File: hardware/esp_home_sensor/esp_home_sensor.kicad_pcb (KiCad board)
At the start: 2 copper layers, 6 parts, among them J2 Conn_01x04_MountingPin, J3 Conn_01x04_MountingPin, J4 Conn_01x08_MountingPin, U6 ESP32-C6-MINI-1, U7 BME680

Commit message: minor update
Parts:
- added BT1: Battery_Cell, Battery:BatteryHolder_Keystone_1042_1x18650, B.Cu at (132.9, 111.5)
- added C1: 1u, Capacitor_SMD:C_0402_1005Metric, F.Cu at (208.3, 120.4)
- added C10: 100n, Capacitor_SMD:C_0402_1005Metric, F.Cu at (166.6, 142.5)
- added C11: 100n, Capacitor_SMD:C_0402_1005Metric, F.Cu at (166.6, 144.5)
- added C12: 4.7u, Capacitor_SMD:C_0402_1005Metric, F.Cu at (205.2, 110.5)
- added C13: 4.7u, Capacitor_SMD:C_0402_1005Metric, F.Cu at (205.2, 112.5)
- added C14: 100n, Capacitor_SMD:C_0402_1005Metric, F.Cu at (176.7, 141.4)
- added C15: 100n, Capacitor_SMD:C_0402_1005Metric, F.Cu at (205.2, 114.4)
- added C16: 100n, Capacitor_SMD:C_0402_1005Metric, F.Cu at (205.2, 116.4)
- added C17: 4.7u, Capacitor_SMD:C_0402_1005Metric, F.Cu at (201.1, 134.3)
- added C18: 10u, Capacitor_SMD:C_0402_1005Metric, F.Cu at (201.1, 136.3)
- added C19: 4.7u, Capacitor_SMD:C_0402_1005Metric, F.Cu at (201.1, 138.3)
- added C2: 1u, Capacitor_SMD:C_0402_1005Metric, F.Cu at (208.3, 122.4)
- added C20: 10u, Capacitor_SMD:C_0402_1005Metric, F.Cu at (201.1, 140.2)
- added C3: 100n, Capacitor_SMD:C_0402_1005Metric, F.Cu at (187.5, 140.7)
- added C4: 100n, Capacitor_SMD:C_0402_1005Metric, F.Cu at (187.5, 142.7)
- added C9: 1u, Capacitor_SMD:C_0402_1005Metric, F.Cu at (205.2, 108.5)
- added D1: LED, LED_SMD:LED_0402_1005Metric, F.Cu at (208.6, 127.5)
- added D2: LED, LED_SMD:LED_0402_1005Metric, F.Cu at (208.6, 129.5)
- added J1: USB_C_Receptacle_USB2.0_16P, Connector_USB:USB_C_Receptacle_GCT_USB4110, F.Cu at (168.2, 100.9)
- added JP1: SolderJumper_3_Bridged12, Jumper:SolderJumper-3_P1.3mm_Bridged12_Pad1.0x1.5mm, F.Cu at (162.3, 138.4)
- added JP2: SolderJumper_3_Bridged12, Jumper:SolderJumper-3_P1.3mm_Bridged12_Pad1.0x1.5mm, F.Cu at (209.4, 109.3)
- added JP3: SolderJumper_3_Bridged12, Jumper:SolderJumper-3_P1.3mm_Bridged12_Pad1.0x1.5mm, F.Cu at (162.3, 142.2)
- added JP4: SolderJumper_3_Bridged12, Jumper:SolderJumper-3_P1.3mm_Bridged12_Pad1.0x1.5mm, F.Cu at (174.5, 138.4)
- added JP6: SolderJumper_2_Bridged, Jumper:SolderJumper-2_P1.3mm_Bridged2Bar_Pad1.0x1.5mm, F.Cu at (204.7, 121.2)
- added JP7: SolderJumper_2_Open, Jumper:SolderJumper-2_P1.3mm_Open_Pad1.0x1.5mm, F.Cu at (208.2, 140.6)
- added JP8: SolderJumper_2_Bridged, Jumper:SolderJumper-2_P1.3mm_Bridged2Bar_Pad1.0x1.5mm, F.Cu at (204.7, 124.7)
- added L1: 2.2u, Inductor_SMD:L_0805_2012Metric, F.Cu at (208.3, 134.7)
- added L2: 2.2u, Inductor_SMD:L_0805_2012Metric, F.Cu at (208.3, 137.5)
- added R1: 680, Resistor_SMD:R_0402_1005Metric, F.Cu at (201.1, 120.4)
- added R10: 1k, Resistor_SMD:R_0402_1005Metric, F.Cu at (184.7, 142.3)
- added R11: 1k, Resistor_SMD:R_0402_1005Metric, F.Cu at (184.7, 144.3)
- added R12: 100k, Resistor_SMD:R_0402_1005Metric, F.Cu at (208.1, 115.9)
- added R13: 5.1k, Resistor_SMD:R_0402_1005Metric, F.Cu at (184.7, 130.4)
- added R14: 5.1k, Resistor_SMD:R_0402_1005Metric, F.Cu at (184.7, 132.4)
- added R15: 270k, Resistor_SMD:R_0402_1005Metric, F.Cu at (204.0, 140.8)
- added R16: 270k, Resistor_SMD:R_0402_1005Metric, F.Cu at (204.0, 142.8)
- added R2: 27k, Resistor_SMD:R_0402_1005Metric, F.Cu at (201.1, 122.4)
- added R3: 10k, Resistor_SMD:R_0402_1005Metric, F.Cu at (201.1, 124.4)
- added R4: 10k, Resistor_SMD:R_0402_1005Metric, F.Cu at (201.1, 126.4)
- added R5: R, Resistor_SMD:R_0402_1005Metric, F.Cu at (201.1, 128.4)
- added R6: R, Resistor_SMD:R_0402_1005Metric, F.Cu at (201.1, 130.3)
- added R7: 15, Resistor_SMD:R_0402_1005Metric, F.Cu at (184.7, 136.4)
- added R8: 100, Resistor_SMD:R_0402_1005Metric, F.Cu at (184.7, 138.4)
- added R9: 15, Resistor_SMD:R_0402_1005Metric, F.Cu at (184.7, 140.3)
- added SW1: SW_Push, Button_Switch_SMD:SW_SPST_Omron_B3FS-101xP, F.Cu at (209.4, 87.9)
- added SW2: SW_Push, Button_Switch_SMD:SW_SPST_Omron_B3FS-101xP, F.Cu at (209.4, 95.8)
- added SW3: SW_Push, Button_Switch_SMD:SW_SPST_Omron_B3FS-101xP, F.Cu at (209.4, 103.6)
- added TH1: NTCSP163JF103FT1H, Resistor_SMD:R_0603_1608Metric, F.Cu at (208.9, 124.6)
- added U1: BQ25170, esp_home_sensor:QFN-8_EP_2x2_Pitch0.5mm, F.Cu at (204.7, 128.7)
- added U10: TPS62840, esp_home_sensor:BGA-6_2x3_1.5x1.2mm, F.Cu at (204.3, 138.2)
- added U2: BQ2970, esp_home_sensor:QFN-8_1.5x1.5_Pitch0.5mm, F.Cu at (190.9, 141.6)
- added U3: IRLHS6276TRPBF, esp_home_sensor:QFN-6_2x2_Pitch0.65mm, F.Cu at (188.3, 137.5)
- added U8: VEML3235, esp_home_sensor:VEML3235, F.Cu at (173.6, 142.3)
- added U9: TPS62840, esp_home_sensor:BGA-6_2x3_1.5x1.2mm, F.Cu at (204.3, 135.0)
- moved D3 84.3 mm to (208.8, 113.2)
- moved U6 55.1 mm to (88.6, 86.0), turned to 90 degrees
- moved J2 39.9 mm to (163.9, 123.2)
- moved J3 39.9 mm to (163.9, 130.8)
- moved J4 39.9 mm to (174.8, 123.2)
- moved U7 34.4 mm to (167.4, 139.2)

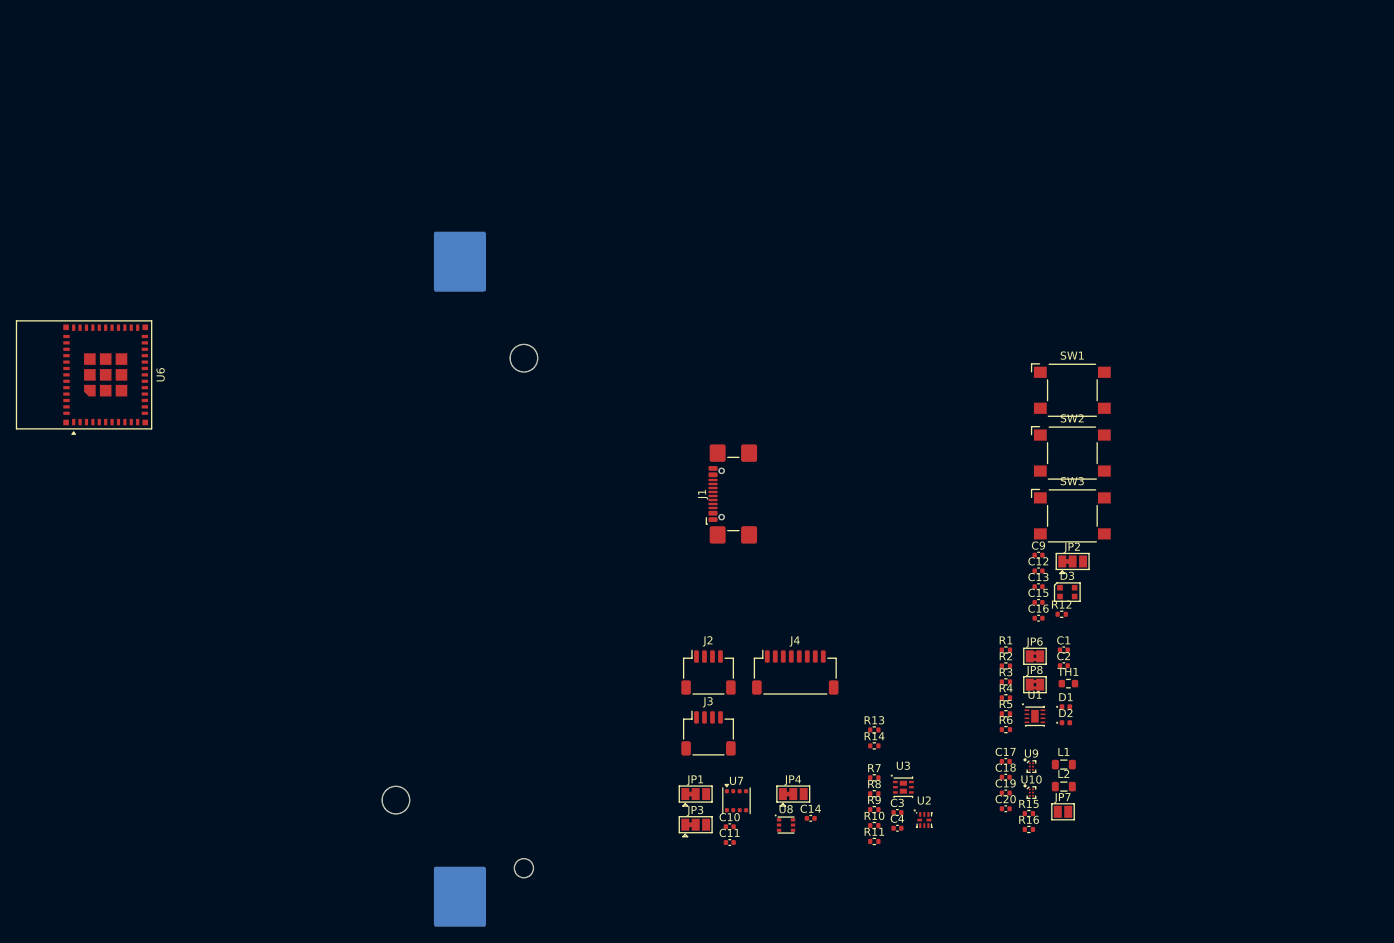
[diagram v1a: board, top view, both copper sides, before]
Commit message: initial layout, power routing
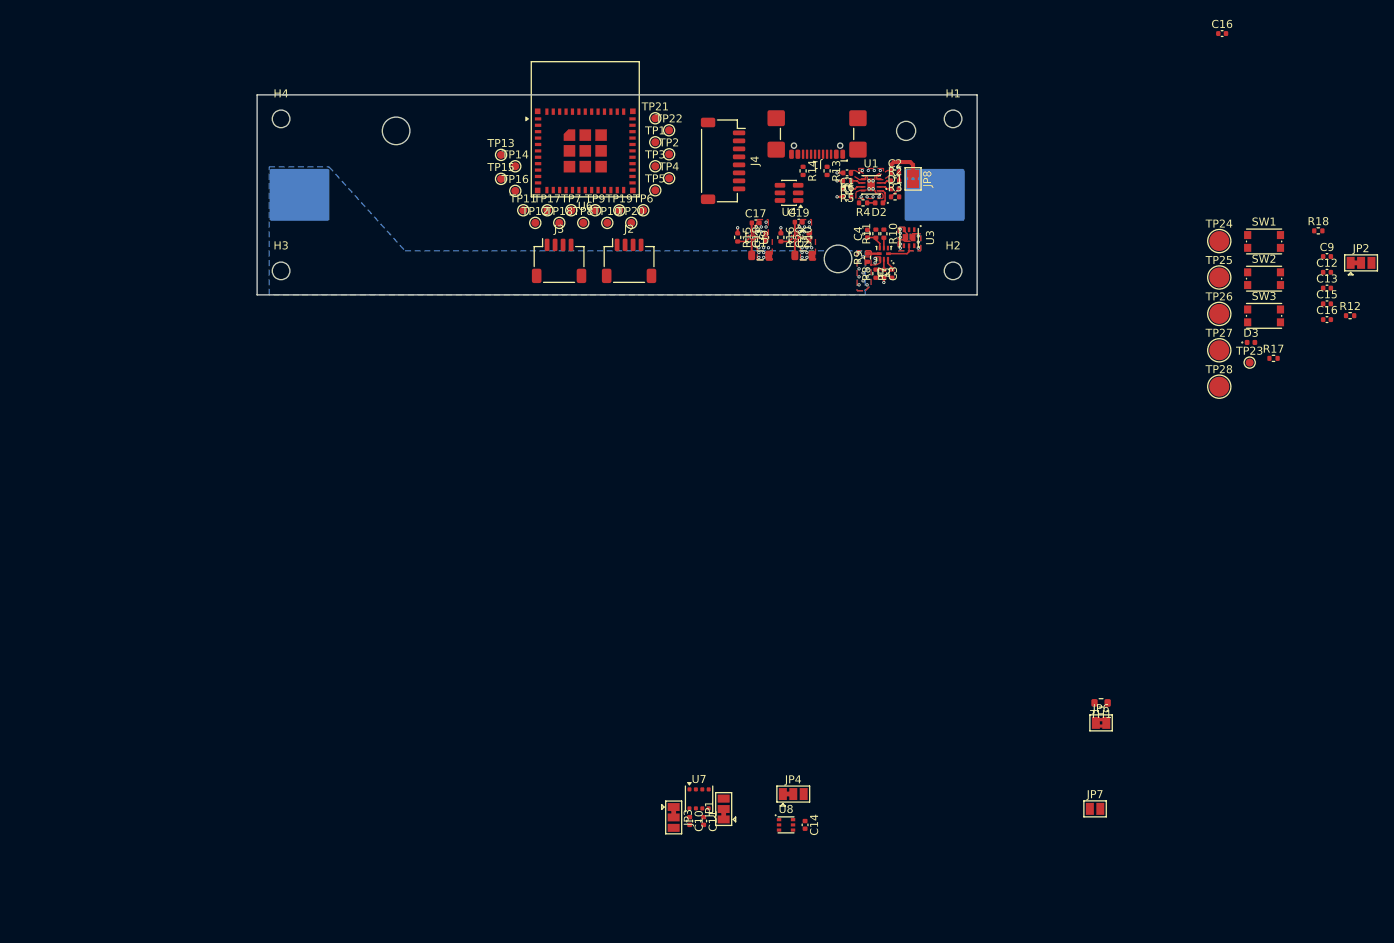
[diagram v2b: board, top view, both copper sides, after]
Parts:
- added C16: 100n, Capacitor_SMD:C_0402_1005Metric, F.Cu at (228.1, 43.3)
- added H1: MountingHole, MountingHole:MountingHole_2.2mm_M2, F.Cu at (194.5, 54.0)
- added H2: MountingHole, MountingHole:MountingHole_2.2mm_M2, F.Cu at (194.5, 73.0)
- added H3: MountingHole, MountingHole:MountingHole_2.2mm_M2, F.Cu at (110.5, 73.0)
- added H4: MountingHole, MountingHole:MountingHole_2.2mm_M2, F.Cu at (110.5, 54.0)
- added R17: 10k, Resistor_SMD:R_0402_1005Metric, F.Cu at (234.6, 83.9)
- added R18: 100, Resistor_SMD:R_0402_1005Metric, F.Cu at (240.2, 68.0)
- added TP1: TestPoint, TestPoint:TestPoint_Pad_D1.0mm, F.Cu at (157.3, 56.9)
- added TP10: TestPoint, TestPoint:TestPoint_Pad_D1.0mm, F.Cu at (151.3, 67.0)
- added TP11: TestPoint, TestPoint:TestPoint_Pad_D1.0mm, F.Cu at (140.8, 65.4)
- added TP12: TestPoint, TestPoint:TestPoint_Pad_D1.0mm, F.Cu at (142.3, 67.0)
- added TP13: TestPoint, TestPoint:TestPoint_Pad_D1.0mm, F.Cu at (138.0, 58.5)
- added TP14: TestPoint, TestPoint:TestPoint_Pad_D1.0mm, F.Cu at (139.8, 59.9)
- added TP15: TestPoint, TestPoint:TestPoint_Pad_D1.0mm, F.Cu at (138.0, 61.5)
- added TP16: TestPoint, TestPoint:TestPoint_Pad_D1.0mm, F.Cu at (139.8, 63.0)
- added TP17: TestPoint, TestPoint:TestPoint_Pad_D1.0mm, F.Cu at (143.8, 65.4)
- added TP18: TestPoint, TestPoint:TestPoint_Pad_D1.0mm, F.Cu at (145.3, 67.0)
- added TP19: TestPoint, TestPoint:TestPoint_Pad_D1.0mm, F.Cu at (152.8, 65.4)
- added TP2: TestPoint, TestPoint:TestPoint_Pad_D1.0mm, F.Cu at (159.0, 58.4)
- added TP20: TestPoint, TestPoint:TestPoint_Pad_D1.0mm, F.Cu at (154.3, 67.0)
- added TP21: TestPoint, TestPoint:TestPoint_Pad_D1.0mm, F.Cu at (157.3, 53.9)
- added TP22: TestPoint, TestPoint:TestPoint_Pad_D1.0mm, F.Cu at (159.0, 55.4)
- added TP23: TestPoint, TestPoint:TestPoint_Pad_D1.0mm, F.Cu at (231.6, 84.5)
- added TP24: TestPoint, TestPoint:TestPoint_Pad_D2.5mm, F.Cu at (227.8, 69.3)
- added TP25: TestPoint, TestPoint:TestPoint_Pad_D2.5mm, F.Cu at (227.8, 73.8)
- added TP26: TestPoint, TestPoint:TestPoint_Pad_D2.5mm, F.Cu at (227.8, 78.4)
- added TP27: TestPoint, TestPoint:TestPoint_Pad_D2.5mm, F.Cu at (227.8, 82.9)
- added TP28: TestPoint, TestPoint:TestPoint_Pad_D2.5mm, F.Cu at (227.8, 87.5)
- added TP3: TestPoint, TestPoint:TestPoint_Pad_D1.0mm, F.Cu at (157.3, 59.9)
- added TP4: TestPoint, TestPoint:TestPoint_Pad_D1.0mm, F.Cu at (159.0, 61.4)
- added TP5: TestPoint, TestPoint:TestPoint_Pad_D1.0mm, F.Cu at (157.3, 62.9)
- added TP6: TestPoint, TestPoint:TestPoint_Pad_D1.0mm, F.Cu at (155.8, 65.4)
- added TP7: TestPoint, TestPoint:TestPoint_Pad_D1.0mm, F.Cu at (146.8, 65.4)
- added TP8: TestPoint, TestPoint:TestPoint_Pad_D1.0mm, F.Cu at (148.3, 67.0)
- added TP9: TestPoint, TestPoint:TestPoint_Pad_D1.0mm, F.Cu at (149.8, 65.4)
- added U4: WE-TVS-82400102, Package_TO_SOT_SMD:SOT-23-6, F.Cu at (174.0, 63.2)
- D3: value WS2812B-2020 -> LED; footprint LED_SMD:LED_WS2812B-2020_PLCC4_2.0x2.0mm -> LED_SMD:LED_0402_1005Metric
- SW1, SW2, SW3: footprint Button_Switch_SMD:SW_SPST_Omron_B3FS-101xP -> Button_Switch_SMD:SW_Push_1P1T_NO_CK_KMR2
- moved R15 80.7 mm to (167.6, 68.8), turned to -90 degrees
- moved R16 80.2 mm to (173.0, 68.8), turned to -90 degrees
- moved R11 76.0 mm to (184.8, 68.3), turned to 90 degrees
- moved C19 75.9 mm to (175.2, 66.9)
- moved C20 75.5 mm to (176.5, 68.8), turned to 90 degrees
- moved U10 75.4 mm to (174.7, 68.8), turned to -90 degrees
- moved U9 74.8 mm to (169.3, 68.8), turned to -90 degrees
- moved C4 74.4 mm to (183.8, 68.3), turned to 90 degrees
- moved C17 74.2 mm to (169.8, 67.0)
- moved L1 74.1 mm to (170.4, 71.1)
- moved R10 74.0 mm to (185.8, 68.3), turned to -90 degrees
- moved L2 74.0 mm to (175.8, 71.1)
- moved C18 73.9 mm to (171.1, 68.8), turned to 90 degrees
- moved R14 72.4 mm to (175.8, 60.5), turned to -90 degrees
- moved U2 71.0 mm to (185.8, 70.8), turned to 180 degrees
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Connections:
- net /MCU/3V3_EN renamed /DC_DC/EN
- net Net-(J1-CC1) renamed /USB/usb_cc1
- net Net-(J1-CC2) renamed /USB/usb_cc2
- net Net-(JP1-C) renamed /Env_sensor/sdo
- net Net-(U1-ISET) renamed /Charger/ISET
- net Net-(U1-VSET) renamed /Charger/VSET
- net Net-(U2-BAT) renamed /Protection/BAT
- net Net-(U2-CHG) renamed /Protection/CHG
- net Net-(U2-CTR) renamed /Protection/CTR
- net Net-(U2-DSG) renamed /Protection/DSG
- net Net-(U2-PACK) renamed /Protection/PACK
- net Net-(U2-VDD) renamed /Protection/VDD
- C2 pad 1: VBAT -> /Charger/OUT
- D3 pad 1: unconnected-(D3-DOUT-Pad1) -> /MCU/USER_LED
- D3 pad 2: GND -> Net-(D3-A)
- J1 pad A6: /MCU/USB.USB_P -> /USB/USB_P
- J1 pad A7: /MCU/USB.USB_N -> /USB/USB_N
- J1 pad B6: /MCU/USB.USB_P -> /USB/USB_P
- J1 pad B7: /MCU/USB.USB_N -> /USB/USB_N
- JP8 pad 1: Net-(JP8-A) -> /Charger/OUT
- L1 pad 1: Net-(U9-SW) -> /DC_DC/SW
- L2 pad 1: Net-(U10-SW) -> /DC_DC/SW
- R15 pad 2: Net-(U9-VSET) -> /DC_DC/VSET
- R16 pad 2: Net-(U10-VSET) -> /DC_DC/VSET
- R3 pad 2: Net-(JP8-A) -> /Charger/OUT
- R4 pad 2: Net-(JP8-A) -> /Charger/OUT
- U1 pad 8: Net-(JP8-A) -> /Charger/OUT
- U10 pad 2B: Net-(U10-SW) -> /DC_DC/SW
- U10 pad 2C: Net-(U10-VSET) -> /DC_DC/VSET
- U6 pad 10: unconnected-(U6-IO5-Pad10) -> /MCU/IO5
- U6 pad 12: /MCU/LED_DATA -> /MCU/USER_LED
- U6 pad 15: unconnected-(U6-IO6-Pad15) -> /MCU/IO6
- U6 pad 16: unconnected-(U6-IO7-Pad16) -> /MCU/IO7
- U6 pad 22: unconnected-(U6-IO8-Pad22) -> /MCU/IO8
- U6 pad 5: VBAT -> /MCU/ADC_BAT
- U6 pad 9: unconnected-(U6-IO4-Pad9) -> /MCU/IO4
- U9 pad 2B: Net-(U9-SW) -> /DC_DC/SW
- U9 pad 2C: Net-(U9-VSET) -> /DC_DC/VSET
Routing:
- net GND: track 0.00 -> 6.00 mm, vias 0 -> 33
- net /Charger/OUT: track 0.00 -> 5.13 mm
- net /DC_DC/SW: track 0.00 -> 4.10 mm
- net /Protection/CHG: track 0.00 -> 3.43 mm
- net VBAT: track 0.00 -> 3.40 mm, vias 0 -> 3
- net /DC_DC/VSET: track 0.00 -> 2.96 mm
- net /Charger/TS: track 0.00 -> 2.59 mm
- net /Protection/CTR: track 0.00 -> 2.55 mm
- net /Protection/VDD: track 0.00 -> 2.33 mm
- net /Charger/STAT: track 0.00 -> 2.21 mm
- net /Charger//PG: track 0.00 -> 1.62 mm
- net /Charger/VSET: track 0.00 -> 1.59 mm
- net /Charger/ISET: track 0.00 -> 1.59 mm
- net /Protection/BAT: track 0.00 -> 1.49 mm
- net /Protection/BAT-: track 0.00 -> 1.48 mm, vias 0 -> 11
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- added copper zone on F.Cu, net /Charger/OUT
- added copper zone on F.Cu, net /Charger/VIN
- added copper zone on B.Cu, net /Protection/BAT-
- added copper zone on F.Cu, net /Protection/BAT-
- added copper zone on F.Cu, net 3V3_AUX
- added copper zone on F.Cu, net 3V3_MCU
- added copper zone on F.Cu, net GND
- added copper zone on In1.Cu, net GND
- added copper zone on B.Cu, net Net-(U3-Pad4)
- added copper zone on F.Cu, net Net-(U3-Pad4)
- added copper zone on In2.Cu, net Net-(U3-Pad4)
- added copper zone on B.Cu, net VBAT
- added copper zone on F.Cu, net VBAT
- added copper zone on In2.Cu, net VBAT
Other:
- board outline added: 90 x 25 mm
- copper layers 2 -> 4
- rule pad_to_mask_clearance: 0 -> 0.05

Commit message: layout
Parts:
- removed the C16 at (241.2, 79.1)
- removed JP2: SolderJumper_3_Bridged12, Jumper:SolderJumper-3_P1.3mm_Bridged12_Pad1.0x1.5mm
- removed TP26: TestPoint, TestPoint:TestPoint_Pad_D2.5mm
- added TP29: TestPoint, TestPoint:TestPoint_Pad_D2.5mm, F.Cu at (115.5, 54.0)
- added TP30: TestPoint, TestPoint:TestPoint_Pad_D2.5mm, F.Cu at (162.5, 73.8)
- TH1: moved to B.Cu
- moved R12 109.8 mm to (136.0, 59.5)
- moved C9 105.8 mm to (136.0, 60.5), turned to 180 degrees
- moved C15 104.9 mm to (136.5, 72.0), turned to -90 degrees
- moved R18 103.0 mm to (137.8, 56.8), turned to 180 degrees
- moved C13 102.8 mm to (140.5, 54.6), turned to 180 degrees
- moved C12 102.3 mm to (140.5, 55.6), turned to 180 degrees
- moved R17 98.6 mm to (137.7, 65.7), turned to -90 degrees
- moved TP23 94.8 mm to (140.0, 60.0)
- moved C14 94.7 mm to (130.3, 59.3), turned to 90 degrees
- moved D3 94.4 mm to (138.7, 65.7), turned to -90 degrees
- moved SW3 93.6 mm to (140.0, 72.0), turned to 180 degrees
- moved JP4 91.4 mm to (128.0, 59.8), turned to 90 degrees
- moved U8 90.9 mm to (131.0, 62.0), turned to 90 degrees
- moved C10 90.5 mm to (121.1, 60.8), turned to 180 degrees
- moved JP1 90.4 mm to (118.5, 63.2)
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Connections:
- L1 pad 1: /DC_DC/SW -> /DC_DC/SW_mcu
- L2 pad 1: /DC_DC/SW -> /DC_DC/SW_aux
- TP25 pad 1: /MCU/PROG_RX -> 3V3_AUX
- U10 pad 2B: /DC_DC/SW -> /DC_DC/SW_aux
- U4 pad 1: /USB/USB_P -> /USB/USB_N
- U4 pad 3: /USB/USB_N -> /USB/USB_P
- U4 pad 4: /MCU/USB.USB_N -> /MCU/USB.USB_P
- U4 pad 6: /MCU/USB.USB_P -> /MCU/USB.USB_N
- U9 pad 2B: /DC_DC/SW -> /DC_DC/SW_mcu
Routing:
- net VBAT: track 3.40 -> 85.9 mm, vias 3 -> 6
- net /Env_sensor/I2C.SCL: track 0.00 -> 67.1 mm, vias 0 -> 2
- net /Env_sensor/I2C.SDA: track 0.00 -> 63.1 mm, vias 0 -> 2
- net /DC_DC/EN: track 0.00 -> 40.9 mm, vias 0 -> 2
- net GND: track 6.00 -> 42.7 mm, vias 33 -> 91
- net /MCU/USB.USB_N: track 0.00 -> 36.2 mm
- net /MCU/USB.USB_P: track 0.00 -> 35.5 mm
- net 3V3_AUX: track 0.00 -> 29.5 mm, vias 7 -> 11
- net /MCU/EN: track 0.00 -> 24.6 mm, vias 0 -> 2
- net /MCU/USER_SW: track 0.00 -> 23.2 mm, vias 0 -> 2
- net /MCU/DISP_IF.CLK: track 0.00 -> 18.2 mm, vias 0 -> 2
- net /Charger/VIN: track 0.00 -> 16.3 mm
- net /MCU/BOOT: track 0.00 -> 15.2 mm, vias 0 -> 2
- net /MCU/DISP_IF.BUSY: track 0.00 -> 14.9 mm
- net /MCU/DISP_IF.MOSI: track 0.00 -> 14.6 mm
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- added copper zone on B.Cu, net /Protection/BAT+
- added copper zone on F.Cu, net /Protection/BAT+
- added copper zone on In2.Cu, net 3V3_AUX
- added copper zone on In2.Cu, net 3V3_MCU
- added copper zone on B.Cu, net GND
- added copper zone on In2.Cu, net GND

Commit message: layout
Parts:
- renumbered C9 to C10, C15 to C11, C11 to C14, C10 to C15, C14 to C16, C17 to C5, C19 to C6, C18 to C7, C20 to C8, C16 to C9, J2 to J1, J3 to J2, J4 to J3, J1 to J4, JP6 to JP1, JP8 to JP2, JP7 to JP3, JP3 to JP4, JP1 to JP5, JP4 to JP6, R18 to R1, R7 to R10, R10 to R12, R15 to R13, R16 to R14, R12 to R15, R17 to R16, R13 to R17, R14 to R18, R1 to R2, R6 to R3, R5 to R4, R3 to R5, R4 to R6, R2 to R7, SW2 to SW1, SW1 to SW2, TP28 to TP1, TP13 to TP10, TP14 to TP11, TP15 to TP12, TP16 to TP13, TP17 to TP14, TP18 to TP15, TP19 to TP16, TP20 to TP17, TP21 to TP18, TP22 to TP19, TP30 to TP2, TP7 to TP20, TP8 to TP21, TP9 to TP22, TP10 to TP23, TP6 to TP24, TP5 to TP25, TP4 to TP26, TP3 to TP27, TP2 to TP28, TP1 to TP29, TP27 to TP3, TP29 to TP4, TP25 to TP5, TP24 to TP6, TP23 to TP7, TP11 to TP8, TP12 to TP9, U9 to U4, U10 to U5, U4 to U9
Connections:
- R13 pad 2: /DC_DC/VSET -> /DC_DC/VSET_mcu
- R14 pad 2: /DC_DC/VSET -> /DC_DC/VSET_aux
- U4 pad 2C: /DC_DC/VSET -> /DC_DC/VSET_mcu
- U5 pad 2C: /DC_DC/VSET -> /DC_DC/VSET_aux
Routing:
- net /DC_DC/VSET: track 2.96 -> 0.00 mm
- net /DC_DC/VSET_mcu: track 0.00 -> 1.48 mm
- net /DC_DC/VSET_aux: track 0.00 -> 1.48 mm
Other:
- board text added: "3V3 AUX"
- board text added: "3V3 MCU"
- board text added: "EN"
- board text added: "ESP32 Env Sens Kamil Chaj Mar 2026"
- board text added: "GND"
- board text added: "IO0"
- board text added: "IO1"
- board text added: "IO12"
- board text added: "IO13"
- board text added: "IO14"
- board text added: "IO15"
- board text added: "IO18"
- board text added: "IO19"
- board text added: "IO2"
- board text added: "IO20"
- board text added: "IO21"
- board text added: "IO22"
- board text added: "IO23"
- board text added: "IO3"
- board text added: "IO4"
- board text added: "IO5"
- board text added: "IO6"
- board text added: "IO7"
- board text added: "IO8"
- board text added: "IO9"
- board text added: "RXD0"
- board text added: "TXD0"
- board text added: "VBAT"

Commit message: tutel
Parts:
- added G***: LOGO, LOGO, F.Cu at (132.8, 54.8)
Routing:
- net GND: vias 91 -> 93
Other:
- outline, holes or cut-outs redrawn
- board text added: "BOOT"
- board text added: "DEBUG"
- board text added: "ESP32 Home Sensor Kamil Chaj Mar 2026"
- board text added: "RESET"
- board text added: "STAT"
- board text added: "USER"
- board text added: "~{PG}"
- board text removed: "ESP32 Env Sens Kamil Chaj Mar 2026"

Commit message: in production
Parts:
- added TP30: TestPoint, TestPoint:TestPoint_Pad_D2.5mm, F.Cu at (186.2, 53.5)
- BT1: footprint Battery:BatteryHolder_Keystone_1042_1x18650 -> esp_home_sensor:18650_cage
- moved G*** 0.90 mm to (132.8, 55.6)
- turned BT1 to 0 degrees
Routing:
- net /Charger/VIN: track 16.3 -> 26.0 mm
- net /Protection/BAT+: track 8.42 -> 5.92 mm
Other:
- board text added: "VBUS USB"
